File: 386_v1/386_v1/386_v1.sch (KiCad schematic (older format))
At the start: 68 parts, among them U1 74LVC1G17GW, U2 74LVC1G17GW, U3 i386SX, U7 Conn_02x32_Odd_Even, U8 Conn_02x32_Odd_Even

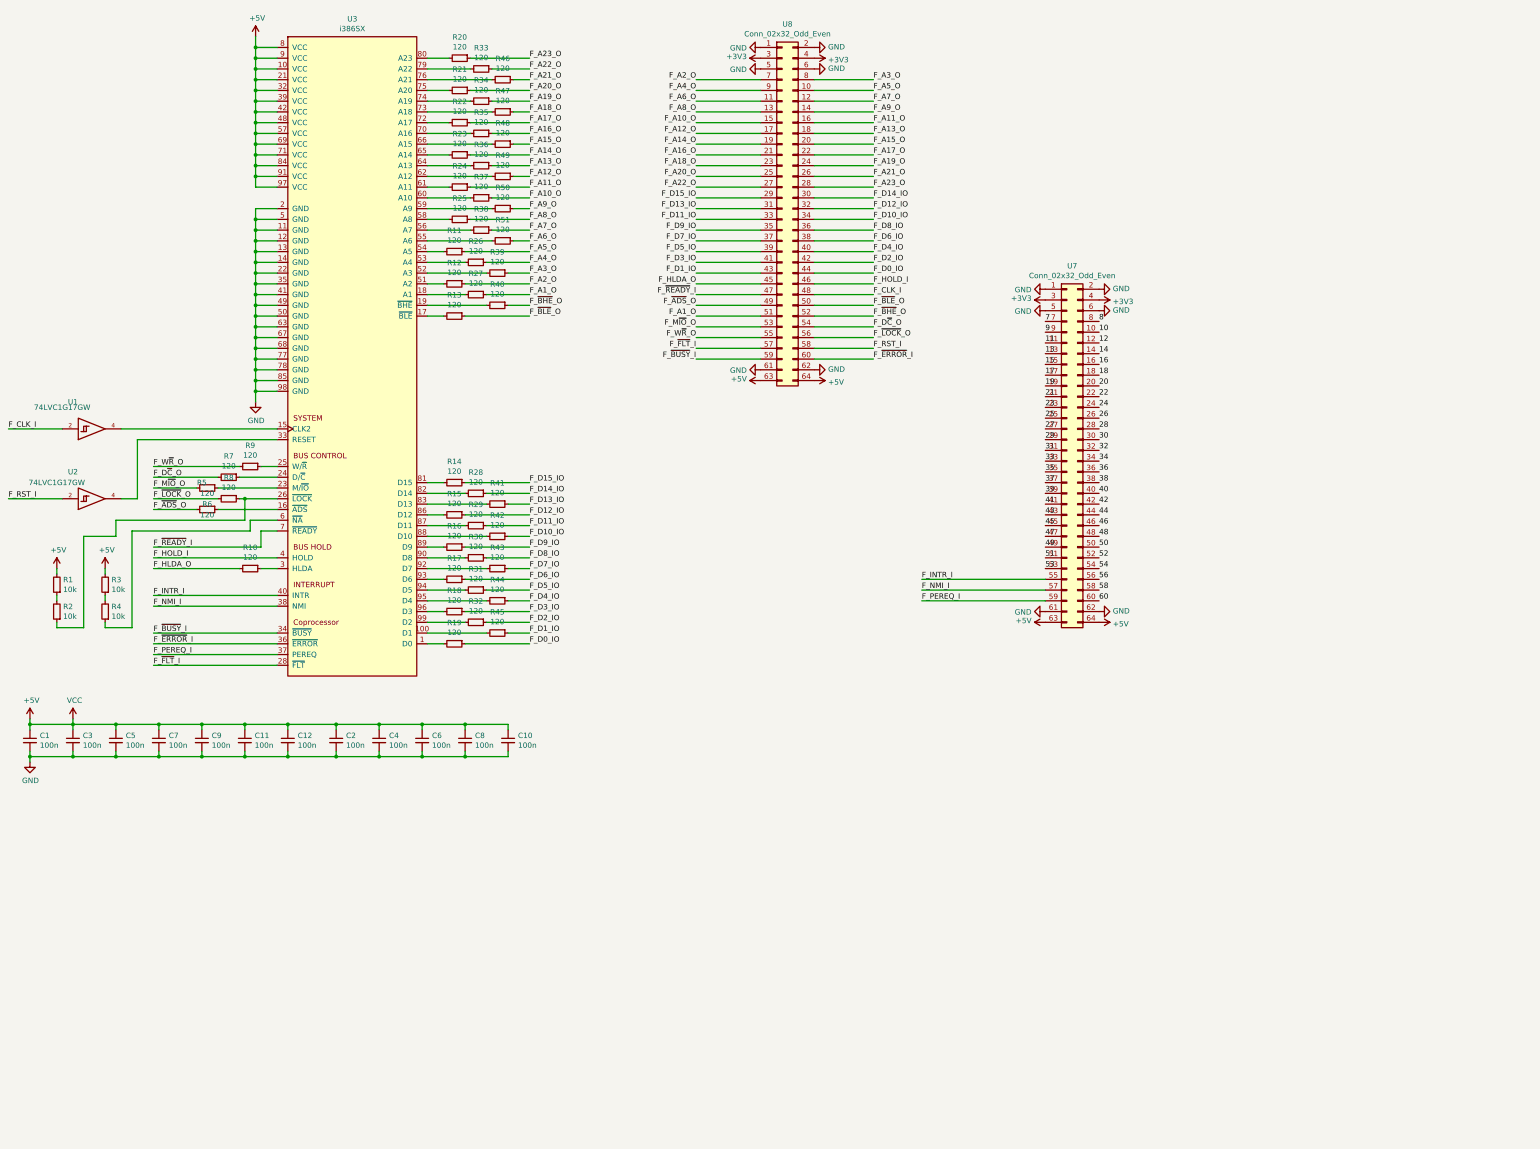
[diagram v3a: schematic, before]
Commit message: update schematic, use active level shifters
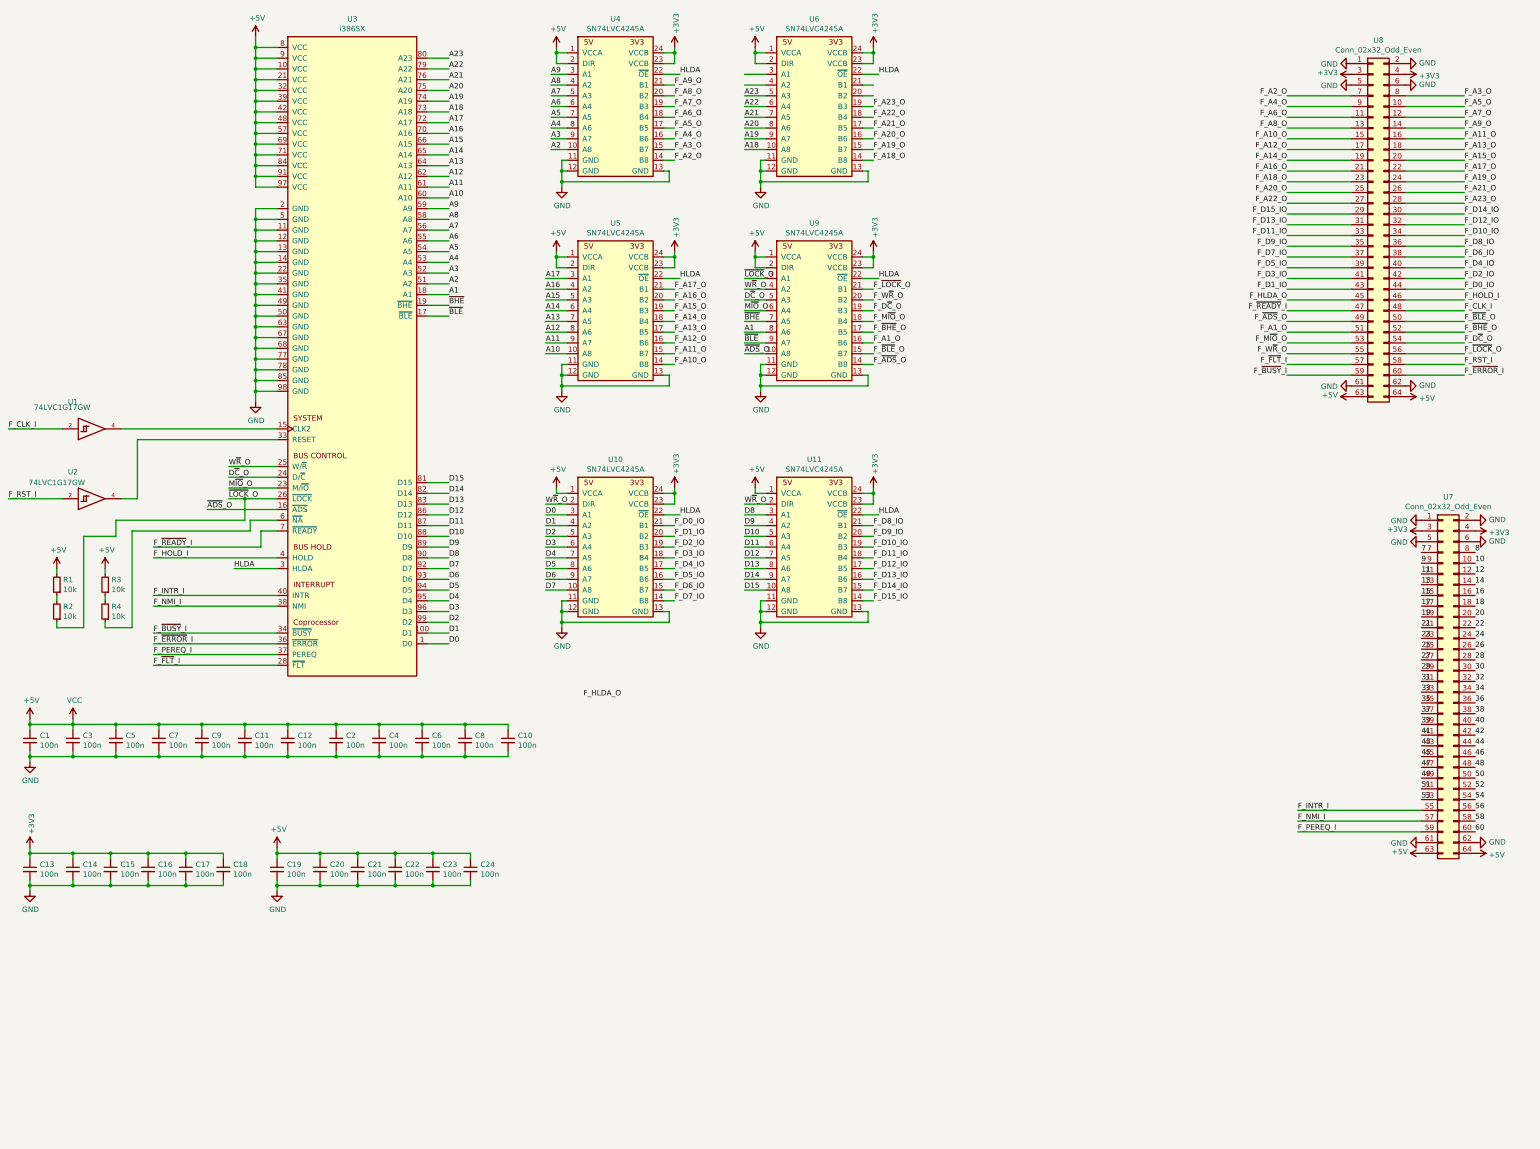
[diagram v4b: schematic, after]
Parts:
- removed R10, R11, R12, R13, R14, R15, R16, R17, R18, R19, R20, R21, R22, R23, R24, R25, R26, R27, R28, R29, R30, R31, R32, R33, R34, R35, R36, R37, R38, R39, R40, R41, R42, R43, R44, R45, R46, R47, R48, R49, R5, R50, R51, R6, R7, R8, R9: 120, Resistor_SMD:R_0805_2012Metric, symbol Device:R_Small
- added C13, C14, C15, C16, C17, C18, C19, C20, C21, C22, C23, C24: 100n, Capacitor_SMD:C_0805_2012Metric_Pad1.15x1.40mm_HandSolder, symbol Device:C_Small
- added U10, U11, U4, U5, U6, U9: SN74LVC4245A, Package_SO:TSSOP-24_4.4x7.8mm_P0.65mm, symbol 386_v1:SN74LVC4245A
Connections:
- net +3V3: now also C13.1, C14.1, C15.1, C16.1, C17.1, C18.1, U10.23 (VCCB), U10.24 (VCCB), U11.23 (VCCB), U11.24 (VCCB), U4.23 (VCCB), U4.24 (VCCB), U5.23 (VCCB), U5.24 (VCCB), U6.23 (VCCB), U6.24 (VCCB), U9.23 (VCCB), U9.24 (VCCB)
- net +5V: now also C19.1, C20.1, C21.1, C22.1, C23.1, C24.1, U10.1 (VCCA), U11.1 (VCCA), U4.1 (VCCA), U4.2 (DIR), U5.1 (VCCA), U5.2 (DIR), U6.1 (VCCA), U6.2 (DIR), U9.1 (VCCA), U9.2 (DIR)
- net F_A10_O: now also U5.14 (B8)
- net F_A11_O: now also U5.15 (B7)
- net F_A12_O: now also U5.16 (B6)
- net F_A13_O: now also U5.17 (B5)
- net F_A14_O: now also U5.18 (B4)
- net F_A15_O: now also U5.19 (B3)
- net F_A16_O: now also U5.20 (B2)
- net F_A17_O: now also U5.21 (B1)
- net F_A18_O: now also U6.14 (B8)
- net F_A19_O: now also U6.15 (B7)
- net F_A1_O: now also U9.16 (B6)
- net F_A20_O: now also U6.16 (B6)
- net F_A21_O: now also U6.17 (B5)
- net F_A22_O: now also U6.18 (B4)
- net F_A23_O: now also U6.19 (B3)
- net F_A2_O: now also U4.14 (B8)
- net F_A3_O: now also U4.15 (B7)
- net F_A4_O: now also U4.16 (B6)
- net F_A5_O: now also U4.17 (B5)
- net F_A6_O: now also U4.18 (B4)
- net F_A7_O: now also U4.19 (B3)
- net F_A8_O: now also U4.20 (B2)
- net F_A9_O: now also U4.21 (B1)
- net F_D0_IO: now also U10.21 (B1)
- net F_D10_IO: now also U11.19 (B3)
- net F_D11_IO: now also U11.18 (B4)
- net F_D12_IO: now also U11.17 (B5)
- net F_D13_IO: now also U11.16 (B6)
- net F_D14_IO: now also U11.15 (B7)
- net F_D15_IO: now also U11.14 (B8)
- net F_D1_IO: now also U10.20 (B2)
- net F_D2_IO: now also U10.19 (B3)
- net F_D3_IO: now also U10.18 (B4)
- net F_D4_IO: now also U10.17 (B5)
- net F_D5_IO: now also U10.16 (B6)
- net F_D6_IO: now also U10.15 (B7)
- net F_D7_IO: now also U10.14 (B8)
- net F_D8_IO: now also U11.21 (B1)
- net F_D9_IO: now also U11.20 (B2)
- net F_D~C~_O: now also U9.19 (B3)
- net F_M~IO~_O: now also U9.18 (B4)
- net F_W~R~_O: now also U9.20 (B2)
- net F_~ADS~_O: now also U9.14 (B8)
- net F_~BHE~_O: now also U9.17 (B5)
- net F_~BLE~_O: now also U9.15 (B7)
- net F_~LOCK~_O: now also U9.21 (B1)
- net GND: now also C13.2, C14.2, C15.2, C16.2, C17.2, C18.2, C19.2, C20.2, C21.2, C22.2, C23.2, C24.2, U10.11 (GND), U10.12 (GND), U10.13 (GND), U11.11 (GND), U11.12 (GND), U11.13 (GND), U4.11 (GND), U4.12 (GND), U4.13 (GND), U5.11 (GND), U5.12 (GND), U5.13 (GND), U6.11 (GND), U6.12 (GND), U6.13 (GND), U9.11 (GND), U9.12 (GND), U9.13 (GND)
- net D0: now reaches U3.1 (D0)
- net D0: now also U10.3 (A1)
- net D1: now reaches U3.100 (D1)
- net D1: now also U10.4 (A2)
- net ~ADS~_O: now reaches U3.16 (~ADS)
- net ~ADS~_O: now also U9.10 (A8)
- net ~BLE: now reaches U3.17 (~BLE)
- net ~BLE: now also U9.9 (A7)
- net A1: now reaches U3.18 (A1)
- net A1: now also U9.8 (A6)
- net ~BHE: now reaches U3.19 (~BHE)
- net ~BHE: now also U9.7 (A5)
- net M~IO~_O: now reaches U3.23 (M/~IO)
- net M~IO~_O: now also U9.6 (A4)
- net D~C~_O: now reaches U3.24 (D/~C)
- net D~C~_O: now also U9.5 (A3)
- net W~R~_O: now reaches U3.25 (W/~R)
- net W~R~_O: now also U10.2 (DIR), U11.2 (DIR), U9.4 (A2)
- net ~LOCK~_O: now reaches R2.1, U3.26 (~LOCK)
- net ~LOCK~_O: now also U9.3 (A1)
- net HLDA: now reaches U3.3 (HLDA)
- net HLDA: now also U10.22 (~OE), U11.22 (~OE), U4.22 (~OE), U5.22 (~OE), U6.22 (~OE), U9.22 (~OE)
- net A2: now reaches U3.51 (A2)
- net A2: now also U4.10 (A8)
- net A3: now reaches U3.52 (A3)
- net A3: now also U4.9 (A7)
- net A4: now reaches U3.53 (A4)
- net A4: now also U4.8 (A6)
- net A5: now reaches U3.54 (A5)
- net A5: now also U4.7 (A5)
- net A6: now reaches U3.55 (A6)
- net A6: now also U4.6 (A4)
- net A7: now reaches U3.56 (A7)
- net A7: now also U4.5 (A3)
- net A8: now reaches U3.58 (A8)
- net A8: now also U4.4 (A2)
- net A9: now reaches U3.59 (A9)
- net A9: now also U4.3 (A1)
- net A10: now reaches U3.60 (A10)
- net A10: now also U5.10 (A8)
- net A11: now reaches U3.61 (A11)
- net A11: now also U5.9 (A7)
- net A12: now reaches U3.62 (A12)
- net A12: now also U5.8 (A6)
- net A13: now reaches U3.64 (A13)
- net A13: now also U5.7 (A5)
- net A14: now reaches U3.65 (A14)
- net A14: now also U5.6 (A4)
- net A15: now reaches U3.66 (A15)
- net A15: now also U5.5 (A3)
- net A16: now reaches U3.70 (A16)
- net A16: now also U5.4 (A2)
- net A17: now reaches U3.72 (A17)
- net A17: now also U5.3 (A1)
- net A18: now reaches U3.73 (A18)
- net A18: now also U6.10 (A8)
- net A19: now reaches U3.74 (A19)
- net A19: now also U6.9 (A7)
- net A20: now reaches U3.75 (A20)
- net A20: now also U6.8 (A6)
- net A21: now reaches U3.76 (A21)
- net A21: now also U6.7 (A5)
- net A22: now reaches U3.79 (A22)
- net A22: now also U6.6 (A4)
- net A23: now reaches U3.80 (A23)
- net A23: now also U6.5 (A3)
- net D15: now reaches U3.81 (D15)
- net D15: now also U11.10 (A8)
- net D14: now reaches U3.82 (D14)
- net D14: now also U11.9 (A7)
- net D13: now reaches U3.83 (D13)
- net D13: now also U11.8 (A6)
- net D12: now reaches U3.86 (D12)
- net D12: now also U11.7 (A5)
- net D11: now reaches U3.87 (D11)
- net D11: now also U11.6 (A4)
- net D10: now reaches U3.88 (D10)
- net D10: now also U11.5 (A3)
- net D9: now reaches U3.89 (D9)
- net D9: now also U11.4 (A2)
- net D8: now reaches U3.90 (D8)
- net D8: now also U11.3 (A1)
- net D7: now reaches U3.92 (D7)
- net D7: now also U10.10 (A8)
- net D6: now reaches U3.93 (D6)
- net D6: now also U10.9 (A7)
- net D5: now reaches U3.94 (D5)
- net D5: now also U10.8 (A6)
- net D4: now reaches U3.95 (D4)
- net D4: now also U10.7 (A5)
- net D3: now reaches U3.96 (D3)
- net D3: now also U10.6 (A4)
- net D2: now reaches U3.99 (D2)
- net D2: now also U10.5 (A3)
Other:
- moved on the sheet: U7, U8

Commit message: pcb with buffers
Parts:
- added U12, U13: 74LVC1G17GW, Package_SO:TSOP-5_1.65x3.05mm_P0.95mm, symbol 74xGxx:74LVC1G17
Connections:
- net +5V: now also U12.5 (VCC), U13.5 (VCC)
- net F_A10_O: now also U8.17 (Pin_17); no longer U8.15 (Pin_15)
- net F_A11_O: now also U8.20 (Pin_20); no longer U8.16 (Pin_16)
- net F_A12_O: now also U8.19 (Pin_19); no longer U8.17 (Pin_17)
- net F_A13_O: now also U8.22 (Pin_22); no longer U8.18 (Pin_18)
- net F_A14_O: now also U8.21 (Pin_21); no longer U8.19 (Pin_19)
- net F_A15_O: now also U8.24 (Pin_24); no longer U8.20 (Pin_20)
- net F_A16_O: now also U8.23 (Pin_23); no longer U8.21 (Pin_21)
- net F_A17_O: now also U8.26 (Pin_26); no longer U8.22 (Pin_22)
- net F_A18_O: now also U8.25 (Pin_25); no longer U8.23 (Pin_23)
- net F_A19_O: now also U8.28 (Pin_28); no longer U8.24 (Pin_24)
- net F_A1_O: now also U8.7 (Pin_7); no longer U8.51 (Pin_51)
- net F_A20_O: now also U8.27 (Pin_27); no longer U8.25 (Pin_25)
- net F_A21_O: now also U8.30 (Pin_30); no longer U8.26 (Pin_26)
- net F_A22_O: now also U8.29 (Pin_29); no longer U8.27 (Pin_27)
- net F_A23_O: now also U8.32 (Pin_32); no longer U8.28 (Pin_28)
- net F_A2_O: now also U8.9 (Pin_9); no longer U8.7 (Pin_7)
- net F_A3_O: now also U8.12 (Pin_12); no longer U8.8 (Pin_8)
- net F_A4_O: now also U8.11 (Pin_11); no longer U8.9 (Pin_9)
- net F_A5_O: now also U8.14 (Pin_14); no longer U8.10 (Pin_10)
- net F_A6_O: now also U8.13 (Pin_13); no longer U8.11 (Pin_11)
- net F_A7_O: now also U8.16 (Pin_16); no longer U8.12 (Pin_12)
- net F_A8_O: now also U8.15 (Pin_15); no longer U8.13 (Pin_13)
- net F_A9_O: now also U8.18 (Pin_18); no longer U8.14 (Pin_14)
- net F_CLK_I: now also U8.52 (Pin_52); no longer U8.48 (Pin_48)
- net F_D0_IO: now also U8.47 (Pin_47); no longer U8.44 (Pin_44)
- net F_D10_IO: now also U8.37 (Pin_37); no longer U8.34 (Pin_34)
- net F_D11_IO: now also U8.38 (Pin_38); no longer U8.33 (Pin_33)
- net F_D12_IO: now also U8.35 (Pin_35); no longer U8.32 (Pin_32)
- net F_D13_IO: now also U8.36 (Pin_36); no longer U8.31 (Pin_31)
- net F_D14_IO: now also U8.33 (Pin_33); no longer U8.30 (Pin_30)
- net F_D15_IO: now also U8.34 (Pin_34); no longer U8.29 (Pin_29)
- net F_D1_IO: now also U8.48 (Pin_48); no longer U8.43 (Pin_43)
- net F_D2_IO: now also U8.45 (Pin_45); no longer U8.42 (Pin_42)
- net F_D3_IO: now also U8.46 (Pin_46); no longer U8.41 (Pin_41)
- net F_D4_IO: now also U8.43 (Pin_43); no longer U8.40 (Pin_40)
- net F_D5_IO: now also U8.44 (Pin_44); no longer U8.39 (Pin_39)
- net F_D6_IO: now also U8.41 (Pin_41); no longer U8.38 (Pin_38)
- net F_D7_IO: now also U8.42 (Pin_42); no longer U8.37 (Pin_37)
- net F_D8_IO: now also U8.39 (Pin_39); no longer U8.36 (Pin_36)
- net F_D9_IO: now also U8.40 (Pin_40); no longer U8.35 (Pin_35)
- net F_HLDA_O: now also U10.22 (~OE), U11.22 (~OE), U4.22 (~OE), U5.22 (~OE), U6.22 (~OE), U8.31 (Pin_31), U9.22 (~OE), U12.4; no longer U8.45 (Pin_45)
- net F_HOLD_I: now also U8.50 (Pin_50); no longer U8.46 (Pin_46)
- net F_~ADS~_O: now also U8.51 (Pin_51); no longer U8.49 (Pin_49)
- net F_~BHE~_O: now also U8.10 (Pin_10); no longer U8.52 (Pin_52)
- net F_~BLE~_O: now also U8.8 (Pin_8); no longer U8.50 (Pin_50)
- net F_~READY~_I: now also U8.49 (Pin_49); no longer U8.47 (Pin_47)
- net GND: now also U6.3 (A1), U6.4 (A2), U12.3 (GND), U13.3 (GND)
- net W~R~_O: now also U13.4; no longer U3.25 (W/~R)
- removed net HLDA: U10.22 (~OE), U11.22 (~OE), U3.3 (HLDA), U4.22 (~OE), U5.22 (~OE), U6.22 (~OE), U9.22 (~OE)
- new net HLDA_RAW: U12.2, U3.3 (HLDA)
- new net W~R~_O_RAW: U13.2, U3.25 (W/~R)
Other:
- moved on the sheet: U11, U6, U9
